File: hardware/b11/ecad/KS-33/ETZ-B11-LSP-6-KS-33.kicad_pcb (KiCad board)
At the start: 2 copper layers, 163.9 x 90.2 mm, 0 parts

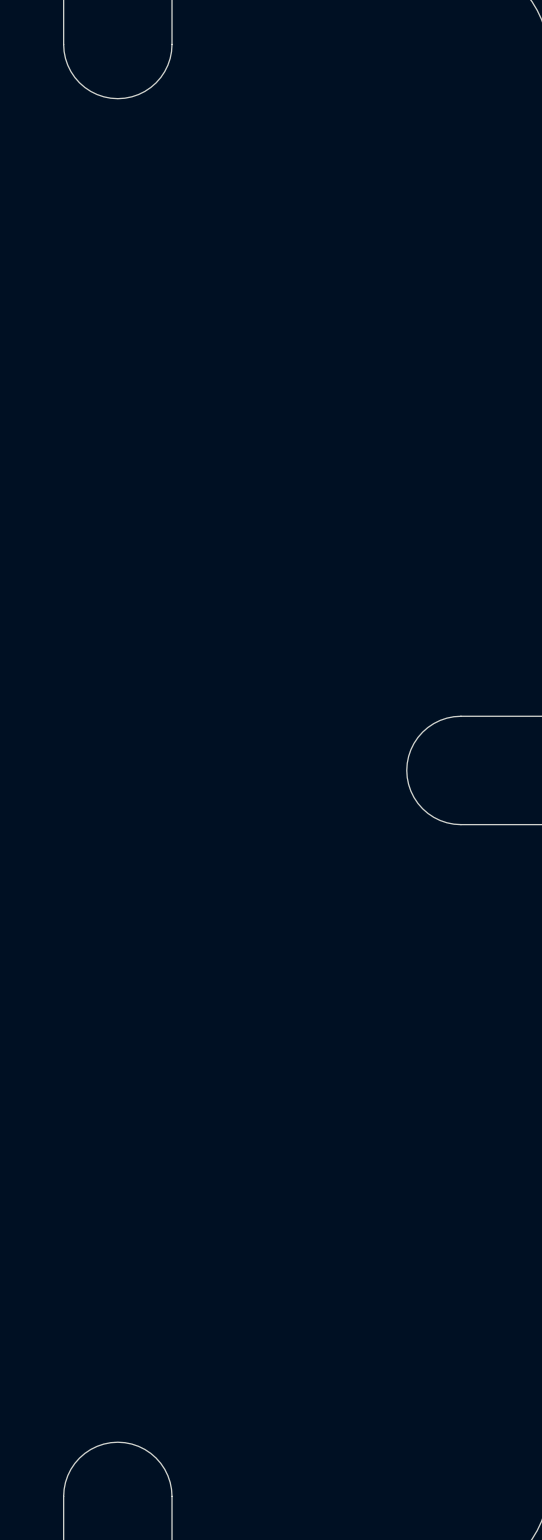
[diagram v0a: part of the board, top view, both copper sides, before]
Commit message: Add B11 display LED placement and stackups
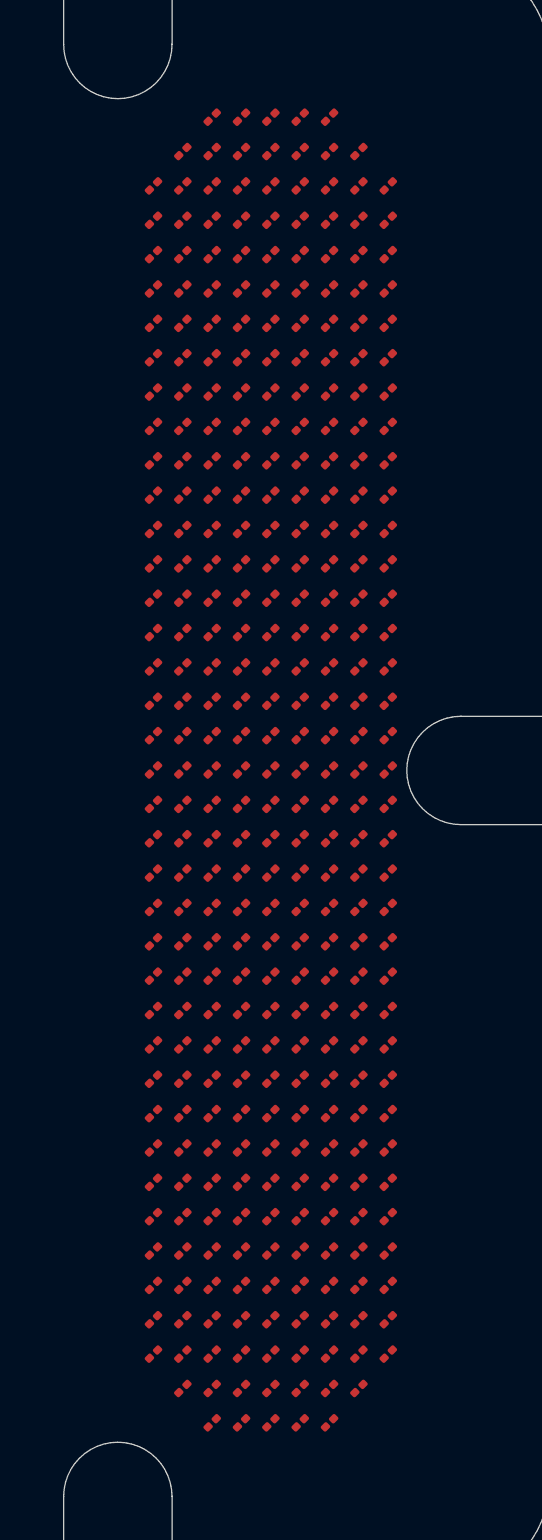
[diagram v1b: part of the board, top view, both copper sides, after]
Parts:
- added D1: 0201_LED, 0201_LED, F.Cu at (211.8, 68.1)
- added D10: 0201_LED, 0201_LED, F.Cu at (216.7, 70.0)
- added D100: 0201_LED, 0201_LED, F.Cu at (218.3, 89.1)
- added D101: 0201_LED, 0201_LED, F.Cu at (219.9, 89.1)
- added D102: 0201_LED, 0201_LED, F.Cu at (221.5, 89.1)
- added D103: 0201_LED, 0201_LED, F.Cu at (208.5, 91.0)
- added D104: 0201_LED, 0201_LED, F.Cu at (210.2, 91.0)
- added D105: 0201_LED, 0201_LED, F.Cu at (211.8, 91.0)
- added D106: 0201_LED, 0201_LED, F.Cu at (213.4, 91.0)
- added D107: 0201_LED, 0201_LED, F.Cu at (215.0, 91.0)
- added D108: 0201_LED, 0201_LED, F.Cu at (216.7, 91.0)
- added D109: 0201_LED, 0201_LED, F.Cu at (218.3, 91.0)
- added D11: 0201_LED, 0201_LED, F.Cu at (218.3, 70.0)
- added D110: 0201_LED, 0201_LED, F.Cu at (219.9, 91.0)
- added D111: 0201_LED, 0201_LED, F.Cu at (221.5, 91.0)
- added D112: 0201_LED, 0201_LED, F.Cu at (208.5, 92.9)
- added D113: 0201_LED, 0201_LED, F.Cu at (210.2, 92.9)
- added D114: 0201_LED, 0201_LED, F.Cu at (211.8, 92.9)
- added D115: 0201_LED, 0201_LED, F.Cu at (213.4, 92.9)
- added D116: 0201_LED, 0201_LED, F.Cu at (215.0, 92.9)
- added D117: 0201_LED, 0201_LED, F.Cu at (216.7, 92.9)
- added D118: 0201_LED, 0201_LED, F.Cu at (218.3, 92.9)
- added D119: 0201_LED, 0201_LED, F.Cu at (219.9, 92.9)
- added D12: 0201_LED, 0201_LED, F.Cu at (219.9, 70.0)
- added D120: 0201_LED, 0201_LED, F.Cu at (221.5, 92.9)
- added D121: 0201_LED, 0201_LED, F.Cu at (208.5, 94.8)
- added D122: 0201_LED, 0201_LED, F.Cu at (210.2, 94.8)
- added D123: 0201_LED, 0201_LED, F.Cu at (211.8, 94.8)
- added D124: 0201_LED, 0201_LED, F.Cu at (213.4, 94.8)
- added D125: 0201_LED, 0201_LED, F.Cu at (215.0, 94.8)
- added D126: 0201_LED, 0201_LED, F.Cu at (216.7, 94.8)
- added D127: 0201_LED, 0201_LED, F.Cu at (218.3, 94.8)
- added D128: 0201_LED, 0201_LED, F.Cu at (219.9, 94.8)
- added D129: 0201_LED, 0201_LED, F.Cu at (221.5, 94.8)
- added D13: 0201_LED, 0201_LED, F.Cu at (208.5, 71.9)
- added D130: 0201_LED, 0201_LED, F.Cu at (208.5, 96.7)
- added D131: 0201_LED, 0201_LED, F.Cu at (210.2, 96.7)
- added D132: 0201_LED, 0201_LED, F.Cu at (211.8, 96.7)
- added D133: 0201_LED, 0201_LED, F.Cu at (213.4, 96.7)
- added D134: 0201_LED, 0201_LED, F.Cu at (215.0, 96.7)
- added D135: 0201_LED, 0201_LED, F.Cu at (216.7, 96.7)
- added D136: 0201_LED, 0201_LED, F.Cu at (218.3, 96.7)
- added D137: 0201_LED, 0201_LED, F.Cu at (219.9, 96.7)
- added D138: 0201_LED, 0201_LED, F.Cu at (221.5, 96.7)
- added D139: 0201_LED, 0201_LED, F.Cu at (208.5, 98.6)
- added D14: 0201_LED, 0201_LED, F.Cu at (210.2, 71.9)
- added D140: 0201_LED, 0201_LED, F.Cu at (210.2, 98.6)
- added D141: 0201_LED, 0201_LED, F.Cu at (211.8, 98.6)
- added D142: 0201_LED, 0201_LED, F.Cu at (213.4, 98.6)
- added D143: 0201_LED, 0201_LED, F.Cu at (215.0, 98.6)
- added D144: 0201_LED, 0201_LED, F.Cu at (216.7, 98.6)
- added D145: 0201_LED, 0201_LED, F.Cu at (218.3, 98.6)
- added D146: 0201_LED, 0201_LED, F.Cu at (219.9, 98.6)
- added D147: 0201_LED, 0201_LED, F.Cu at (221.5, 98.6)
- added D148: 0201_LED, 0201_LED, F.Cu at (208.5, 100.5)
- added D149: 0201_LED, 0201_LED, F.Cu at (210.2, 100.5)
- added D15: 0201_LED, 0201_LED, F.Cu at (211.8, 71.9)
- added D150: 0201_LED, 0201_LED, F.Cu at (211.8, 100.5)
- added D151: 0201_LED, 0201_LED, F.Cu at (213.4, 100.5)
- added D152: 0201_LED, 0201_LED, F.Cu at (215.0, 100.5)
- added D153: 0201_LED, 0201_LED, F.Cu at (216.7, 100.5)
- added D154: 0201_LED, 0201_LED, F.Cu at (218.3, 100.5)
- added D155: 0201_LED, 0201_LED, F.Cu at (219.9, 100.5)
- added D156: 0201_LED, 0201_LED, F.Cu at (221.5, 100.5)
- added D157: 0201_LED, 0201_LED, F.Cu at (208.5, 102.4)
- added D158: 0201_LED, 0201_LED, F.Cu at (210.2, 102.4)
- added D159: 0201_LED, 0201_LED, F.Cu at (211.8, 102.4)
- added D16: 0201_LED, 0201_LED, F.Cu at (213.4, 71.9)
- added D160: 0201_LED, 0201_LED, F.Cu at (213.4, 102.4)
- added D161: 0201_LED, 0201_LED, F.Cu at (215.0, 102.4)
- added D162: 0201_LED, 0201_LED, F.Cu at (216.7, 102.4)
- added D163: 0201_LED, 0201_LED, F.Cu at (218.3, 102.4)
- added D164: 0201_LED, 0201_LED, F.Cu at (219.9, 102.4)
- added D165: 0201_LED, 0201_LED, F.Cu at (221.5, 102.4)
- added D166: 0201_LED, 0201_LED, F.Cu at (208.5, 104.3)
- added D167: 0201_LED, 0201_LED, F.Cu at (210.2, 104.3)
- added D168: 0201_LED, 0201_LED, F.Cu at (211.8, 104.3)
- added D169: 0201_LED, 0201_LED, F.Cu at (213.4, 104.3)
- added D17: 0201_LED, 0201_LED, F.Cu at (215.0, 71.9)
- added D170: 0201_LED, 0201_LED, F.Cu at (215.0, 104.3)
- added D171: 0201_LED, 0201_LED, F.Cu at (216.7, 104.3)
- added D172: 0201_LED, 0201_LED, F.Cu at (218.3, 104.3)
- added D173: 0201_LED, 0201_LED, F.Cu at (219.9, 104.3)
- added D174: 0201_LED, 0201_LED, F.Cu at (221.5, 104.3)
- added D175: 0201_LED, 0201_LED, F.Cu at (208.5, 106.2)
- added D176: 0201_LED, 0201_LED, F.Cu at (210.2, 106.2)
- added D177: 0201_LED, 0201_LED, F.Cu at (211.8, 106.2)
- added D178: 0201_LED, 0201_LED, F.Cu at (213.4, 106.2)
- added D179: 0201_LED, 0201_LED, F.Cu at (215.0, 106.2)
- added D18: 0201_LED, 0201_LED, F.Cu at (216.7, 71.9)
- added D180: 0201_LED, 0201_LED, F.Cu at (216.7, 106.2)
- added D181: 0201_LED, 0201_LED, F.Cu at (218.3, 106.2)
- added D182: 0201_LED, 0201_LED, F.Cu at (219.9, 106.2)
- added D183: 0201_LED, 0201_LED, F.Cu at (221.5, 106.2)
- added D184: 0201_LED, 0201_LED, F.Cu at (208.5, 108.1)
- added D185: 0201_LED, 0201_LED, F.Cu at (210.2, 108.1)
- added D186: 0201_LED, 0201_LED, F.Cu at (211.8, 108.1)
- added D187: 0201_LED, 0201_LED, F.Cu at (213.4, 108.1)
- added D188: 0201_LED, 0201_LED, F.Cu at (215.0, 108.1)
- added D189: 0201_LED, 0201_LED, F.Cu at (216.7, 108.1)
- added D19: 0201_LED, 0201_LED, F.Cu at (218.3, 71.9)
- added D190: 0201_LED, 0201_LED, F.Cu at (218.3, 108.1)
- added D191: 0201_LED, 0201_LED, F.Cu at (219.9, 108.1)
- added D192: 0201_LED, 0201_LED, F.Cu at (221.5, 108.1)
- added D193: 0201_LED, 0201_LED, F.Cu at (208.5, 110.0)
- added D194: 0201_LED, 0201_LED, F.Cu at (210.2, 110.0)
- added D195: 0201_LED, 0201_LED, F.Cu at (211.8, 110.0)
- added D196: 0201_LED, 0201_LED, F.Cu at (213.4, 110.0)
- added D197: 0201_LED, 0201_LED, F.Cu at (215.0, 110.0)
- added D198: 0201_LED, 0201_LED, F.Cu at (216.7, 110.0)
- added D199: 0201_LED, 0201_LED, F.Cu at (218.3, 110.0)
- added D2: 0201_LED, 0201_LED, F.Cu at (213.4, 68.1)
- added D20: 0201_LED, 0201_LED, F.Cu at (219.9, 71.9)
- added D200: 0201_LED, 0201_LED, F.Cu at (219.9, 110.0)
- added D201: 0201_LED, 0201_LED, F.Cu at (221.5, 110.0)
- added D202: 0201_LED, 0201_LED, F.Cu at (208.5, 111.9)
- added D203: 0201_LED, 0201_LED, F.Cu at (210.2, 111.9)
- added D204: 0201_LED, 0201_LED, F.Cu at (211.8, 111.9)
- added D205: 0201_LED, 0201_LED, F.Cu at (213.4, 111.9)
- added D206: 0201_LED, 0201_LED, F.Cu at (215.0, 111.9)
- added D207: 0201_LED, 0201_LED, F.Cu at (216.7, 111.9)
- added D208: 0201_LED, 0201_LED, F.Cu at (218.3, 111.9)
- added D209: 0201_LED, 0201_LED, F.Cu at (219.9, 111.9)
- added D21: 0201_LED, 0201_LED, F.Cu at (221.5, 71.9)
- added D210: 0201_LED, 0201_LED, F.Cu at (221.5, 111.9)
- added D211: 0201_LED, 0201_LED, F.Cu at (208.5, 113.8)
- added D212: 0201_LED, 0201_LED, F.Cu at (210.2, 113.8)
- added D213: 0201_LED, 0201_LED, F.Cu at (211.8, 113.8)
- added D214: 0201_LED, 0201_LED, F.Cu at (213.4, 113.8)
- added D215: 0201_LED, 0201_LED, F.Cu at (215.0, 113.8)
- added D216: 0201_LED, 0201_LED, F.Cu at (216.7, 113.8)
- added D217: 0201_LED, 0201_LED, F.Cu at (218.3, 113.8)
- added D218: 0201_LED, 0201_LED, F.Cu at (219.9, 113.8)
- added D219: 0201_LED, 0201_LED, F.Cu at (221.5, 113.8)
- added D22: 0201_LED, 0201_LED, F.Cu at (208.5, 73.8)
- added D220: 0201_LED, 0201_LED, F.Cu at (208.5, 115.7)
- added D221: 0201_LED, 0201_LED, F.Cu at (210.2, 115.7)
- added D222: 0201_LED, 0201_LED, F.Cu at (211.8, 115.7)
- added D223: 0201_LED, 0201_LED, F.Cu at (213.4, 115.7)
- added D224: 0201_LED, 0201_LED, F.Cu at (215.0, 115.7)
- added D225: 0201_LED, 0201_LED, F.Cu at (216.7, 115.7)
- added D226: 0201_LED, 0201_LED, F.Cu at (218.3, 115.7)
- added D227: 0201_LED, 0201_LED, F.Cu at (219.9, 115.7)
- added D228: 0201_LED, 0201_LED, F.Cu at (221.5, 115.7)
- added D229: 0201_LED, 0201_LED, F.Cu at (208.5, 117.6)
- added D23: 0201_LED, 0201_LED, F.Cu at (210.2, 73.8)
- added D230: 0201_LED, 0201_LED, F.Cu at (210.2, 117.6)
- added D231: 0201_LED, 0201_LED, F.Cu at (211.8, 117.6)
- added D232: 0201_LED, 0201_LED, F.Cu at (213.4, 117.6)
- added D233: 0201_LED, 0201_LED, F.Cu at (215.0, 117.6)
- added D234: 0201_LED, 0201_LED, F.Cu at (216.7, 117.6)
- added D235: 0201_LED, 0201_LED, F.Cu at (218.3, 117.6)
- added D236: 0201_LED, 0201_LED, F.Cu at (219.9, 117.6)
- added D237: 0201_LED, 0201_LED, F.Cu at (221.5, 117.6)
- added D238: 0201_LED, 0201_LED, F.Cu at (208.5, 119.5)
- added D239: 0201_LED, 0201_LED, F.Cu at (210.2, 119.5)
- added D24: 0201_LED, 0201_LED, F.Cu at (211.8, 73.8)
- added D240: 0201_LED, 0201_LED, F.Cu at (211.8, 119.5)
- added D241: 0201_LED, 0201_LED, F.Cu at (213.4, 119.5)
- added D242: 0201_LED, 0201_LED, F.Cu at (215.0, 119.5)
- added D243: 0201_LED, 0201_LED, F.Cu at (216.7, 119.5)
- added D244: 0201_LED, 0201_LED, F.Cu at (218.3, 119.5)
- added D245: 0201_LED, 0201_LED, F.Cu at (219.9, 119.5)
- added D246: 0201_LED, 0201_LED, F.Cu at (221.5, 119.5)
- added D247: 0201_LED, 0201_LED, F.Cu at (208.5, 121.4)
- added D248: 0201_LED, 0201_LED, F.Cu at (210.2, 121.4)
- added D249: 0201_LED, 0201_LED, F.Cu at (211.8, 121.4)
- added D25: 0201_LED, 0201_LED, F.Cu at (213.4, 73.8)
- added D250: 0201_LED, 0201_LED, F.Cu at (213.4, 121.4)
- added D251: 0201_LED, 0201_LED, F.Cu at (215.0, 121.4)
- added D252: 0201_LED, 0201_LED, F.Cu at (216.7, 121.4)
- added D253: 0201_LED, 0201_LED, F.Cu at (218.3, 121.4)
- added D254: 0201_LED, 0201_LED, F.Cu at (219.9, 121.4)
- added D255: 0201_LED, 0201_LED, F.Cu at (221.5, 121.4)
- added D256: 0201_LED, 0201_LED, F.Cu at (208.5, 123.3)
- added D257: 0201_LED, 0201_LED, F.Cu at (210.2, 123.3)
- added D258: 0201_LED, 0201_LED, F.Cu at (211.8, 123.3)
- added D259: 0201_LED, 0201_LED, F.Cu at (213.4, 123.3)
- added D26: 0201_LED, 0201_LED, F.Cu at (215.0, 73.8)
- added D260: 0201_LED, 0201_LED, F.Cu at (215.0, 123.3)
- added D261: 0201_LED, 0201_LED, F.Cu at (216.7, 123.3)
- added D262: 0201_LED, 0201_LED, F.Cu at (218.3, 123.3)
- added D263: 0201_LED, 0201_LED, F.Cu at (219.9, 123.3)
- added D264: 0201_LED, 0201_LED, F.Cu at (221.5, 123.3)
- added D265: 0201_LED, 0201_LED, F.Cu at (208.5, 125.2)
- added D266: 0201_LED, 0201_LED, F.Cu at (210.2, 125.2)
- added D267: 0201_LED, 0201_LED, F.Cu at (211.8, 125.2)
- added D268: 0201_LED, 0201_LED, F.Cu at (213.4, 125.2)
- added D269: 0201_LED, 0201_LED, F.Cu at (215.0, 125.2)
- added D27: 0201_LED, 0201_LED, F.Cu at (216.7, 73.8)
- added D270: 0201_LED, 0201_LED, F.Cu at (216.7, 125.2)
- added D271: 0201_LED, 0201_LED, F.Cu at (218.3, 125.2)
- added D272: 0201_LED, 0201_LED, F.Cu at (219.9, 125.2)
- added D273: 0201_LED, 0201_LED, F.Cu at (221.5, 125.2)
- added D274: 0201_LED, 0201_LED, F.Cu at (208.5, 127.1)
- added D275: 0201_LED, 0201_LED, F.Cu at (210.2, 127.1)
- added D276: 0201_LED, 0201_LED, F.Cu at (211.8, 127.1)
- added D277: 0201_LED, 0201_LED, F.Cu at (213.4, 127.1)
- added D278: 0201_LED, 0201_LED, F.Cu at (215.0, 127.1)
- added D279: 0201_LED, 0201_LED, F.Cu at (216.7, 127.1)
- added D28: 0201_LED, 0201_LED, F.Cu at (218.3, 73.8)
- added D280: 0201_LED, 0201_LED, F.Cu at (218.3, 127.1)
- added D281: 0201_LED, 0201_LED, F.Cu at (219.9, 127.1)
- added D282: 0201_LED, 0201_LED, F.Cu at (221.5, 127.1)
- added D283: 0201_LED, 0201_LED, F.Cu at (208.5, 129.0)
- added D284: 0201_LED, 0201_LED, F.Cu at (210.2, 129.0)
- added D285: 0201_LED, 0201_LED, F.Cu at (211.8, 129.0)
- added D286: 0201_LED, 0201_LED, F.Cu at (213.4, 129.0)
- added D287: 0201_LED, 0201_LED, F.Cu at (215.0, 129.0)
- added D288: 0201_LED, 0201_LED, F.Cu at (216.7, 129.0)
- added D289: 0201_LED, 0201_LED, F.Cu at (218.3, 129.0)
- added D29: 0201_LED, 0201_LED, F.Cu at (219.9, 73.8)
- added D290: 0201_LED, 0201_LED, F.Cu at (219.9, 129.0)
- added D291: 0201_LED, 0201_LED, F.Cu at (221.5, 129.0)
- added D292: 0201_LED, 0201_LED, F.Cu at (208.5, 130.9)
- added D293: 0201_LED, 0201_LED, F.Cu at (210.2, 130.9)
- added D294: 0201_LED, 0201_LED, F.Cu at (211.8, 130.9)
- added D295: 0201_LED, 0201_LED, F.Cu at (213.4, 130.9)
- added D296: 0201_LED, 0201_LED, F.Cu at (215.0, 130.9)
- added D297: 0201_LED, 0201_LED, F.Cu at (216.7, 130.9)
- added D298: 0201_LED, 0201_LED, F.Cu at (218.3, 130.9)
- added D299: 0201_LED, 0201_LED, F.Cu at (219.9, 130.9)
- added D3: 0201_LED, 0201_LED, F.Cu at (215.0, 68.1)
- added D30: 0201_LED, 0201_LED, F.Cu at (221.5, 73.8)
- added D300: 0201_LED, 0201_LED, F.Cu at (221.5, 130.9)
- added D301: 0201_LED, 0201_LED, F.Cu at (208.5, 132.8)
- added D302: 0201_LED, 0201_LED, F.Cu at (210.2, 132.8)
- added D303: 0201_LED, 0201_LED, F.Cu at (211.8, 132.8)
- added D304: 0201_LED, 0201_LED, F.Cu at (213.4, 132.8)
- added D305: 0201_LED, 0201_LED, F.Cu at (215.0, 132.8)
- added D306: 0201_LED, 0201_LED, F.Cu at (216.7, 132.8)
- added D307: 0201_LED, 0201_LED, F.Cu at (218.3, 132.8)
- added D308: 0201_LED, 0201_LED, F.Cu at (219.9, 132.8)
- added D309: 0201_LED, 0201_LED, F.Cu at (221.5, 132.8)
- added D31: 0201_LED, 0201_LED, F.Cu at (208.5, 75.7)
- added D310: 0201_LED, 0201_LED, F.Cu at (208.5, 134.7)
- added D311: 0201_LED, 0201_LED, F.Cu at (210.2, 134.7)
- added D312: 0201_LED, 0201_LED, F.Cu at (211.8, 134.7)
- added D313: 0201_LED, 0201_LED, F.Cu at (213.4, 134.7)
- added D314: 0201_LED, 0201_LED, F.Cu at (215.0, 134.7)
- added D315: 0201_LED, 0201_LED, F.Cu at (216.7, 134.7)
- added D316: 0201_LED, 0201_LED, F.Cu at (218.3, 134.7)
- added D317: 0201_LED, 0201_LED, F.Cu at (219.9, 134.7)
- added D318: 0201_LED, 0201_LED, F.Cu at (221.5, 134.7)
- added D319: 0201_LED, 0201_LED, F.Cu at (208.5, 136.6)
- added D32: 0201_LED, 0201_LED, F.Cu at (210.2, 75.7)
- added D320: 0201_LED, 0201_LED, F.Cu at (210.2, 136.6)
- added D321: 0201_LED, 0201_LED, F.Cu at (211.8, 136.6)
- added D322: 0201_LED, 0201_LED, F.Cu at (213.4, 136.6)
- added D323: 0201_LED, 0201_LED, F.Cu at (215.0, 136.6)
- added D324: 0201_LED, 0201_LED, F.Cu at (216.7, 136.6)
- added D325: 0201_LED, 0201_LED, F.Cu at (218.3, 136.6)
- added D326: 0201_LED, 0201_LED, F.Cu at (219.9, 136.6)
- added D327: 0201_LED, 0201_LED, F.Cu at (221.5, 136.6)
- added D328: 0201_LED, 0201_LED, F.Cu at (210.2, 138.5)
- added D329: 0201_LED, 0201_LED, F.Cu at (211.8, 138.5)
- added D33: 0201_LED, 0201_LED, F.Cu at (211.8, 75.7)
- added D330: 0201_LED, 0201_LED, F.Cu at (213.4, 138.5)
- added D331: 0201_LED, 0201_LED, F.Cu at (215.0, 138.5)
- added D332: 0201_LED, 0201_LED, F.Cu at (216.7, 138.5)
- added D333: 0201_LED, 0201_LED, F.Cu at (218.3, 138.5)
- added D334: 0201_LED, 0201_LED, F.Cu at (219.9, 138.5)
- added D335: 0201_LED, 0201_LED, F.Cu at (211.8, 140.4)
- added D336: 0201_LED, 0201_LED, F.Cu at (213.4, 140.4)
- added D337: 0201_LED, 0201_LED, F.Cu at (215.0, 140.4)
- added D338: 0201_LED, 0201_LED, F.Cu at (216.7, 140.4)
- added D339: 0201_LED, 0201_LED, F.Cu at (218.3, 140.4)
- added D34: 0201_LED, 0201_LED, F.Cu at (213.4, 75.7)
- added D35: 0201_LED, 0201_LED, F.Cu at (215.0, 75.7)
- added D36: 0201_LED, 0201_LED, F.Cu at (216.7, 75.7)
- added D37: 0201_LED, 0201_LED, F.Cu at (218.3, 75.7)
- added D38: 0201_LED, 0201_LED, F.Cu at (219.9, 75.7)
- added D39: 0201_LED, 0201_LED, F.Cu at (221.5, 75.7)
- added D4: 0201_LED, 0201_LED, F.Cu at (216.7, 68.1)
- added D40: 0201_LED, 0201_LED, F.Cu at (208.5, 77.6)
- added D41: 0201_LED, 0201_LED, F.Cu at (210.2, 77.6)
- added D42: 0201_LED, 0201_LED, F.Cu at (211.8, 77.6)
- added D43: 0201_LED, 0201_LED, F.Cu at (213.4, 77.6)
- added D44: 0201_LED, 0201_LED, F.Cu at (215.0, 77.6)
- added D45: 0201_LED, 0201_LED, F.Cu at (216.7, 77.6)
- added D46: 0201_LED, 0201_LED, F.Cu at (218.3, 77.6)
- added D47: 0201_LED, 0201_LED, F.Cu at (219.9, 77.6)
- added D48: 0201_LED, 0201_LED, F.Cu at (221.5, 77.6)
- added D49: 0201_LED, 0201_LED, F.Cu at (208.5, 79.5)
- added D5: 0201_LED, 0201_LED, F.Cu at (218.3, 68.1)
- added D50: 0201_LED, 0201_LED, F.Cu at (210.2, 79.5)
- added D51: 0201_LED, 0201_LED, F.Cu at (211.8, 79.5)
- added D52: 0201_LED, 0201_LED, F.Cu at (213.4, 79.5)
- added D53: 0201_LED, 0201_LED, F.Cu at (215.0, 79.5)
- added D54: 0201_LED, 0201_LED, F.Cu at (216.7, 79.5)
- added D55: 0201_LED, 0201_LED, F.Cu at (218.3, 79.5)
- added D56: 0201_LED, 0201_LED, F.Cu at (219.9, 79.5)
- added D57: 0201_LED, 0201_LED, F.Cu at (221.5, 79.5)
- added D58: 0201_LED, 0201_LED, F.Cu at (208.5, 81.4)
- added D59: 0201_LED, 0201_LED, F.Cu at (210.2, 81.4)
- added D6: 0201_LED, 0201_LED, F.Cu at (210.2, 70.0)
- added D60: 0201_LED, 0201_LED, F.Cu at (211.8, 81.4)
- added D61: 0201_LED, 0201_LED, F.Cu at (213.4, 81.4)
- added D62: 0201_LED, 0201_LED, F.Cu at (215.0, 81.4)
- added D63: 0201_LED, 0201_LED, F.Cu at (216.7, 81.4)
- added D64: 0201_LED, 0201_LED, F.Cu at (218.3, 81.4)
- added D65: 0201_LED, 0201_LED, F.Cu at (219.9, 81.4)
- added D66: 0201_LED, 0201_LED, F.Cu at (221.5, 81.4)
- added D67: 0201_LED, 0201_LED, F.Cu at (208.5, 83.3)
- added D68: 0201_LED, 0201_LED, F.Cu at (210.2, 83.3)
- added D69: 0201_LED, 0201_LED, F.Cu at (211.8, 83.3)
- added D7: 0201_LED, 0201_LED, F.Cu at (211.8, 70.0)
- added D70: 0201_LED, 0201_LED, F.Cu at (213.4, 83.3)
- added D71: 0201_LED, 0201_LED, F.Cu at (215.0, 83.3)
- added D72: 0201_LED, 0201_LED, F.Cu at (216.7, 83.3)
- added D73: 0201_LED, 0201_LED, F.Cu at (218.3, 83.3)
- added D74: 0201_LED, 0201_LED, F.Cu at (219.9, 83.3)
- added D75: 0201_LED, 0201_LED, F.Cu at (221.5, 83.3)
- added D76: 0201_LED, 0201_LED, F.Cu at (208.5, 85.2)
- added D77: 0201_LED, 0201_LED, F.Cu at (210.2, 85.2)
- added D78: 0201_LED, 0201_LED, F.Cu at (211.8, 85.2)
- added D79: 0201_LED, 0201_LED, F.Cu at (213.4, 85.2)
- added D8: 0201_LED, 0201_LED, F.Cu at (213.4, 70.0)
- added D80: 0201_LED, 0201_LED, F.Cu at (215.0, 85.2)
- added D81: 0201_LED, 0201_LED, F.Cu at (216.7, 85.2)
- added D82: 0201_LED, 0201_LED, F.Cu at (218.3, 85.2)
- added D83: 0201_LED, 0201_LED, F.Cu at (219.9, 85.2)
- added D84: 0201_LED, 0201_LED, F.Cu at (221.5, 85.2)
- added D85: 0201_LED, 0201_LED, F.Cu at (208.5, 87.2)
- added D86: 0201_LED, 0201_LED, F.Cu at (210.2, 87.2)
- added D87: 0201_LED, 0201_LED, F.Cu at (211.8, 87.2)
- added D88: 0201_LED, 0201_LED, F.Cu at (213.4, 87.2)
- added D89: 0201_LED, 0201_LED, F.Cu at (215.0, 87.2)
- added D9: 0201_LED, 0201_LED, F.Cu at (215.0, 70.0)
- added D90: 0201_LED, 0201_LED, F.Cu at (216.7, 87.2)
- added D91: 0201_LED, 0201_LED, F.Cu at (218.3, 87.2)
- added D92: 0201_LED, 0201_LED, F.Cu at (219.9, 87.2)
- added D93: 0201_LED, 0201_LED, F.Cu at (221.5, 87.2)
- added D94: 0201_LED, 0201_LED, F.Cu at (208.5, 89.1)
- added D95: 0201_LED, 0201_LED, F.Cu at (210.2, 89.1)
- added D96: 0201_LED, 0201_LED, F.Cu at (211.8, 89.1)
- added D97: 0201_LED, 0201_LED, F.Cu at (213.4, 89.1)
- added D98: 0201_LED, 0201_LED, F.Cu at (215.0, 89.1)
- added D99: 0201_LED, 0201_LED, F.Cu at (216.7, 89.1)
